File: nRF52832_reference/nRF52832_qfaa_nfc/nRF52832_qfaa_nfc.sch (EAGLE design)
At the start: 21 parts, among them U1 NRF52832, X1 32MHz, X2 32.768kHz

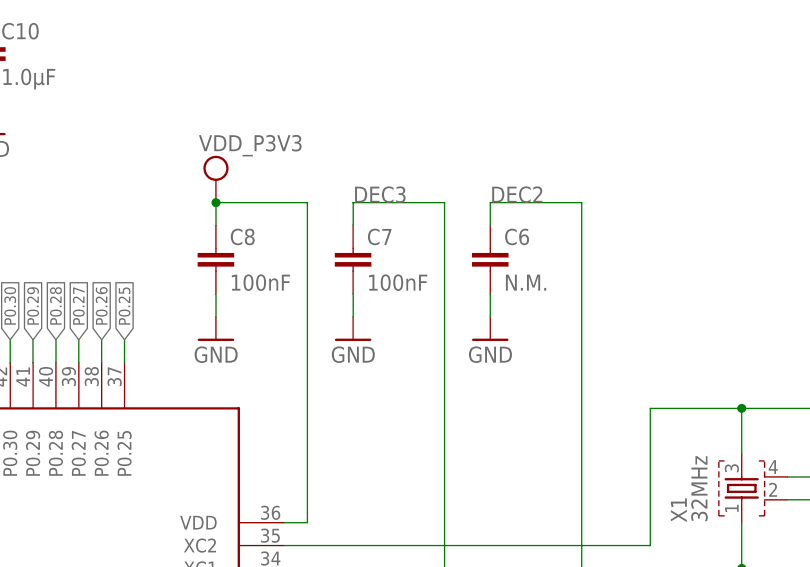
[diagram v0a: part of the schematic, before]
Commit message: Issue #2: Fixed value of C7 from 100nF to 100pF
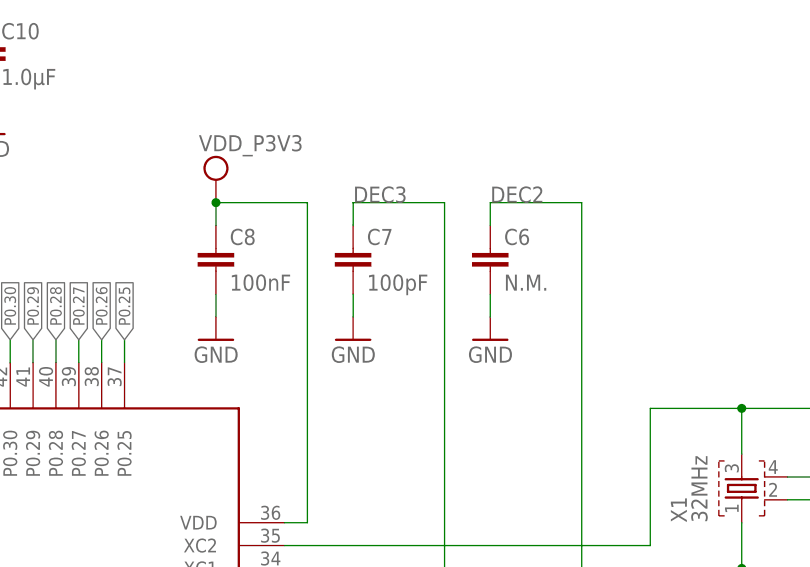
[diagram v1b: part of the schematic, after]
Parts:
- C7: value 100nF -> 100pF
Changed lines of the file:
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@@
 <part name="C5" library="Nordic_nRF" deviceset="CAPACITOR" device="_0402_N" value="100nF"/>
 <part name="C6" library="Nordic_nRF" deviceset="CAPACITOR" device="_0402_N" value="N.M."/>
-<part name="C7" library="Nordic_nRF" deviceset="CAPACITOR" device="_0402_N" value="100nF"/>
+<part name="C7" library="Nordic_nRF" deviceset="CAPACITOR" device="_0402_N" value="100pF"/>
 <part name="C8" library="Nordic_nRF" deviceset="CAPACITOR" device="_0402_N" value="100nF"/>
 <part name="C9" library="Nordic_nRF" deviceset="CAPACITOR" device="_0603_N" value="4.7µF"/>

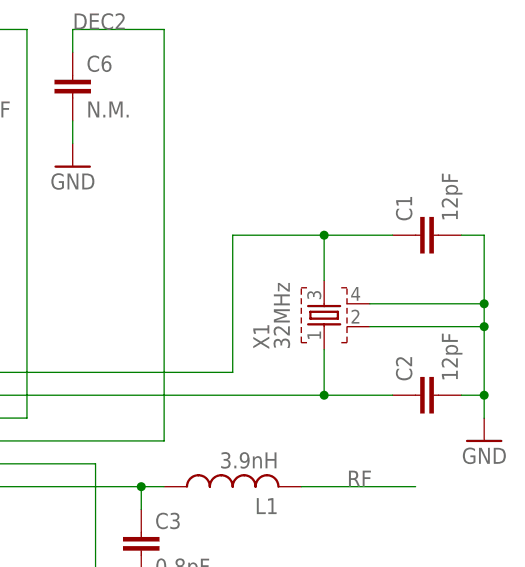
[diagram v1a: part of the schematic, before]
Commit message: Same fixes as in qfaa_dcdc
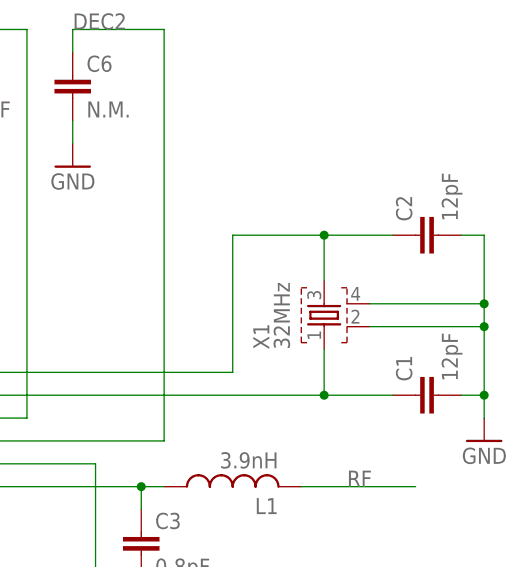
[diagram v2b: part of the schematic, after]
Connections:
- net N$3: now also C2.1; no longer C1.1
- net X1: now also C1.1; no longer C2.1
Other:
- moved on the sheet: C1, C2
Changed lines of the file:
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@@
 <?xml version="1.0" encoding="utf-8"?>
 <!DOCTYPE eagle SYSTEM "eagle.dtd">
-<eagle version="7.6.0">
+<eagle version="8.3.0">
 <drawing>
 <settings>
 <setting alwaysvectorfont="no"/>
+<setting keepoldvectorfont="yes"/>
 <setting verticaltext="up"/>
 </settings>
@@
 <part name="L2" library="Nordic_nRF" deviceset="INDUCTOR" device="_0603_N" value="10µH"/>
 <part name="L3" library="Nordic_nRF" deviceset="INDUCTOR" device="_0402_N" value="15nH"/>
+<part name="C2" library="Nordic_nRF" deviceset="CAPACITOR" device="_0402_N" value="12pF"/>
 <part name="C1" library="Nordic_nRF" deviceset="CAPACITOR" device="_0402_N" value="12pF"/>
-<part name="C2" library="Nordic_nRF" deviceset="CAPACITOR" device="_0402_N" value="12pF"/>
 <part name="C3" library="Nordic_nRF" deviceset="CAPACITOR" device="_0402_N" value="0.8pF"/>
 <part name="C4" library="Nordic_nRF" deviceset="CAPACITOR" device="_0402_N" value="100nF"/>
@@
 <instance part="L3" gate="L$1" x="104.14" y="149.86" rot="R180"/>
 <instance part="L2" gate="L$1" x="104.14" y="134.62" rot="R180"/>
-<instance part="C1" gate="C$1" x="213.36" y="114.3" rot="R90"/>
-<instance part="C2" gate="C$1" x="213.36" y="96.52" rot="R90"/>
+<instance part="C2" gate="C$1" x="213.36" y="114.3" rot="R90"/>
+<instance part="C1" gate="C$1" x="213.36" y="96.52" rot="R90"/>
 <instance part="C3" gate="C$1" x="182.88" y="81.28"/>
 <instance part="C4" gate="C$1" x="68.58" y="132.08"/>
@@
 <pinref part="X1" gate="X$1" pin="4"/>
 <pinref part="X1" gate="X$1" pin="2"/>
+<pinref part="C2" gate="C$1" pin="2"/>
 <pinref part="C1" gate="C$1" pin="2"/>
-<pinref part="C2" gate="C$1" pin="2"/>
 </segment>
 <segment>
@@
 <wire x1="193.04" y1="99.06" x2="152.4" y2="99.06" width="0.1524" layer="91"/>
 <pinref part="X1" gate="X$1" pin="3"/>
-<pinref part="C1" gate="C$1" pin="1"/>
+<pinref part="C2" gate="C$1" pin="1"/>
 </segment>
 </net>
@@
 <junction x="203.2" y="96.52"/>
 <pinref part="X1" gate="X$1" pin="1"/>
-<pinref part="C2" gate="C$1" pin="1"/>
-</segment>
-</net>
+<pinref part="C1" gate="C$1" pin="1"/>
+</segment>
+</net>
